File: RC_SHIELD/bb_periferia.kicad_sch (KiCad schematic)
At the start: 58 parts, among them J10 POWER_SUPPLY, J11 ALF_MOT_DRV, J11 GPIO1, J12 BET_MOT_DRV, J12 GPIO2, J13 SPI, J14 I2C_TEMP, J15 DOOR_SWITCH, J16 ESTOP, J17 FAN, J18 P5a, J9 P4a, Q1 BSS123, Q2 BSS123, U2 SN75LBC179AD, U3 ESP8266-01/ESP-01, U4 LCD-016N002L

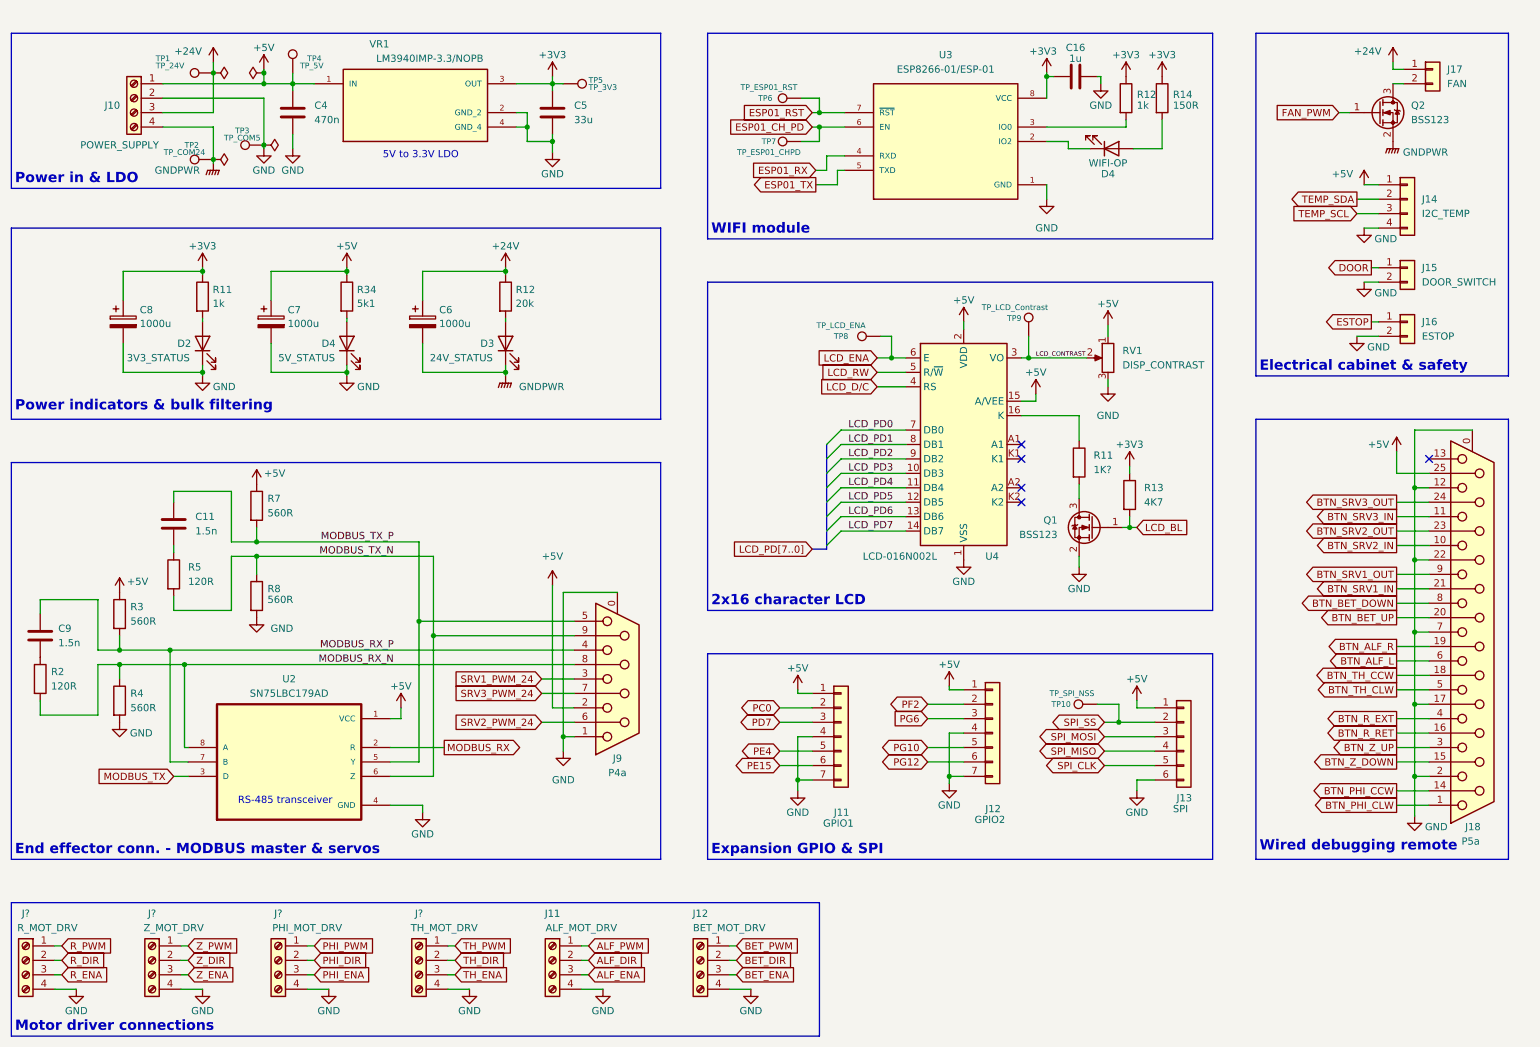
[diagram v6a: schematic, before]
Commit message: [SCH] updated power indicator LED resistor values and tidied up page 3
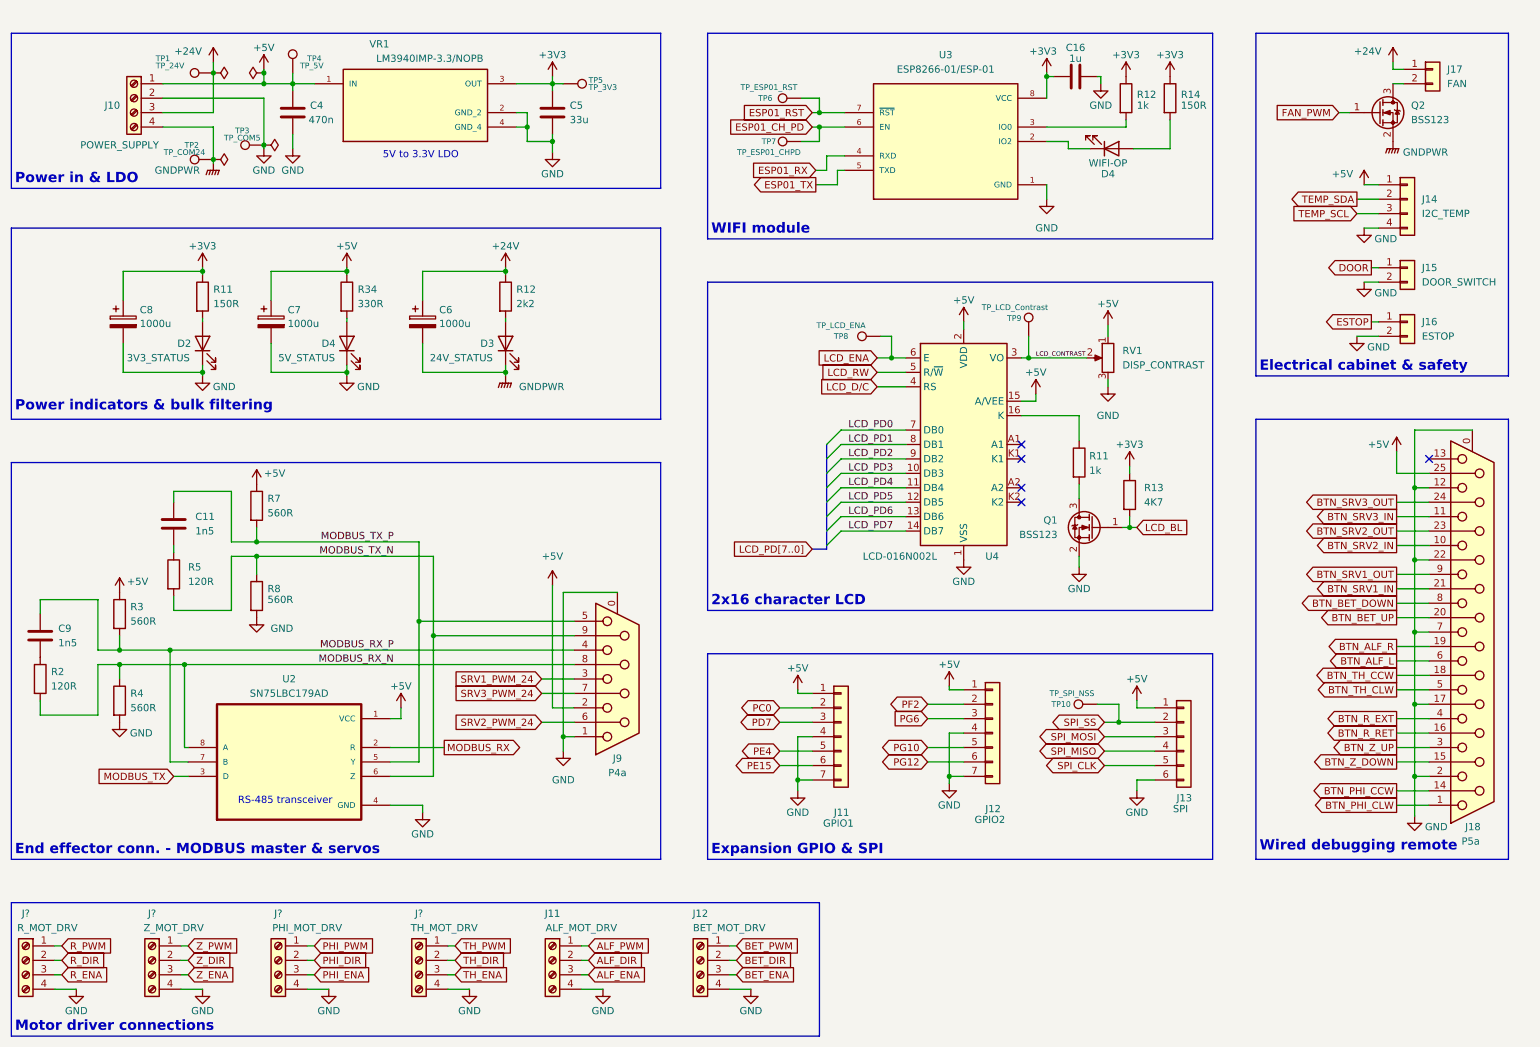
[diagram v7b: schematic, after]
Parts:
- C11, C9: value 1.5n -> 1n5
- D2, D3, D4: footprint Capacitor_SMD:C_0805_2012Metric_Pad1.18x1.45mm_HandSolder -> LED_SMD:LED_0805_2012Metric_Pad1.15x1.40mm_HandSolder
- R11: value 1K? -> 1k; now left out of the parts list
- R11: value 1k -> 150R
- R12: value 20k -> 2k2
- R34: value 5k1 -> 330R
- U3: symbol ESP8266-01_ESP-01:ESP8266-01/ESP-01 -> ESP8266-01_ESP-01:ESP8266-01/ESP-01
- VR1: symbol LM3940IMP-3.3_NOPB:LM3940IMP-3.3/NOPB -> LM3940IMP-3.3_NOPB:LM3940IMP-3.3/NOPB
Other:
- moved on the sheet: R14
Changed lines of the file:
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@@
     (stroke (width 0) (type default))
   )
-  (wire (pts (xy 219.075 31.75) (xy 219.075 36.83))
+  (wire (pts (xy 220.472 31.75) (xy 220.472 36.83))
     (stroke (width 0) (type default))
   )
@@
     (stroke (width 0) (type default))
   )
-  (wire (pts (xy 213.995 36.83) (xy 219.075 36.83))
+  (wire (pts (xy 213.995 36.83) (xy 220.472 36.83))
     (stroke (width 0) (type default))
   )
@@
       (effects (font (size 1.27 1.27)) (justify right))
     )
-    (property "Footprint" "Capacitor_SMD:C_0805_2012Metric_Pad1.18x1.45mm_HandSolder" (at 75.565 71.12 0)
+    (property "Footprint" "LED_SMD:LED_0805_2012Metric_Pad1.15x1.40mm_HandSolder" (at 75.565 71.12 0)
       (effects (font (size 1.27 1.27)) hide)
     )
@@
     )
   )
-  (symbol (lib_id "LM3940IMP-3.3_NOPB:LM3940IMP-3.3{slash}NOPB") (at 87.63 27.94 0) (unit 1)
+  (symbol (lib_id "LM3940IMP-3.3_NOPB:LM3940IMP-3.3/NOPB") (at 87.63 27.94 0) (unit 1)
     (in_bom yes) (on_board yes) (dnp no)
     (property "Reference" "VR1" (at 81.28 18.415 0)
@@
   (symbol (lib_id "Device:R") (at 75.565 62.865 0) (unit 1)
     (in_bom yes) (on_board yes) (dnp no) (fields_autoplaced)
-    (property "Reference" "R34" (at 77.343 61.6529 0)
+    (property "Reference" "R34" (at 77.47 61.595 0)
       (effects (font (size 1.27 1.27)) (justify left))
     )
-    (property "Value" "5k1" (at 77.343 64.0771 0)
+    (property "Value" "330R" (at 77.47 64.135 0)
       (effects (font (size 1.27 1.27)) (justify left))
     )
@@
     )
   )
-  (symbol (lib_id "Device:R") (at 219.075 27.94 0) (unit 1)
+  (symbol (lib_id "Device:R") (at 220.472 27.94 0) (unit 1)
     (in_bom yes) (on_board yes) (dnp no)
-    (property "Reference" "R14" (at 220.98 27.305 0)
+    (property "Reference" "R14" (at 222.377 27.305 0)
       (effects (font (size 1.27 1.27)) (justify left))
     )
-    (property "Value" "150R" (at 220.98 29.21 0)
+    (property "Value" "150R" (at 222.377 29.21 0)
       (effects (font (size 1.27 1.27)) (justify left))
     )
-    (property "Footprint" "Resistor_SMD:R_0805_2012Metric_Pad1.20x1.40mm_HandSolder" (at 217.297 27.94 90)
+    (property "Footprint" "Resistor_SMD:R_0805_2012Metric_Pad1.20x1.40mm_HandSolder" (at 218.694 27.94 90)
       (effects (font (size 1.27 1.27)) hide)
     )
-    (property "Datasheet" "~" (at 219.075 27.94 0)
+    (property "Datasheet" "~" (at 220.472 27.94 0)
       (effects (font (size 1.27 1.27)) hide)
     )
@@
   (symbol (lib_id "Device:R") (at 103.505 62.865 0) (unit 1)
     (in_bom yes) (on_board yes) (dnp no) (fields_autoplaced)
-    (property "Reference" "R12" (at 105.283 61.6529 0)
+    (property "Reference" "R12" (at 105.41 61.595 0)
       (effects (font (size 1.27 1.27)) (justify left))
     )
-    (property "Value" "20k" (at 105.283 64.0771 0)
+    (property "Value" "2k2" (at 105.41 64.135 0)
       (effects (font (size 1.27 1.27)) (justify left))
     )
@@
     )
   )
-  (symbol (lib_id "ESP8266-01_ESP-01:ESP8266-01{slash}ESP-01") (at 180.975 35.56 0) (unit 1)
+  (symbol (lib_id "ESP8266-01_ESP-01:ESP8266-01/ESP-01") (at 180.975 35.56 0) (unit 1)
     (in_bom yes) (on_board yes) (dnp no) (fields_autoplaced)
     (property "Reference" "U3" (at 180.975 20.32 0)
@@
       (effects (font (size 1.27 1.27)) (justify left))
     )
-    (property "Value" "1.5n" (at 24.765 123.825 0)
+    (property "Value" "1n5" (at 24.765 123.825 0)
       (effects (font (size 1.27 1.27)) (justify left))
     )
@@
     )
   )
-  (symbol (lib_id "power:+3V3") (at 219.075 24.13 0) (unit 1)
+  (symbol (lib_id "power:+3V3") (at 220.472 24.13 0) (unit 1)
     (in_bom yes) (on_board yes) (dnp no)
-    (property "Reference" "#PWR065" (at 219.075 27.94 0)
+    (property "Reference" "#PWR065" (at 220.472 27.94 0)
       (effects (font (size 1.27 1.27)) hide)
     )
-    (property "Value" "+3V3" (at 219.075 20.32 0)
+    (property "Value" "+3V3" (at 220.472 20.32 0)
       (effects (font (size 1.27 1.27)))
     )
-    (property "Footprint" "" (at 219.075 24.13 0)
+    (property "Footprint" "" (at 220.472 24.13 0)
       (effects (font (size 1.27 1.27)) hide)
     )
-    (property "Datasheet" "" (at 219.075 24.13 0)
+    (property "Datasheet" "" (at 220.472 24.13 0)
       (effects (font (size 1.27 1.27)) hide)
     )
@@
   )
   (symbol (lib_id "Device:C") (at 111.76 30.48 0) (unit 1)
-    (in_bom yes) (on_board yes) (dnp no) (fields_autoplaced)
-    (property "Reference" "C5" (at 115.57 29.21 0)
+    (in_bom yes) (on_board yes) (dnp no)
+    (property "Reference" "C5" (at 114.808 29.21 0)
       (effects (font (size 1.27 1.27)) (justify left))
     )
-    (property "Value" "33u" (at 115.57 31.75 0)
+    (property "Value" "33u" (at 114.808 31.75 0)
       (effects (font (size 1.27 1.27)) (justify left))
     )
@@
       (effects (font (size 1.27 1.27)))
     )
-    (property "Footprint" "Capacitor_SMD:C_0805_2012Metric_Pad1.18x1.45mm_HandSolder" (at 210.185 36.83 0)
+    (property "Footprint" "LED_SMD:LED_0805_2012Metric_Pad1.15x1.40mm_HandSolder" (at 210.185 36.83 0)
       (effects (font (size 1.27 1.27)) hide)
     )
@@
   )
   (symbol (lib_id "Device:R") (at 204.47 92.075 0) (unit 1)
-    (in_bom yes) (on_board yes) (dnp no) (fields_autoplaced)
-    (property "Reference" "R11" (at 207.01 90.805 0)
+    (in_bom no) (on_board yes) (dnp no)
+    (property "Reference" "R11" (at 206.248 90.932 0)
       (effects (font (size 1.27 1.27)) (justify left))
     )
-    (property "Value" "1K?" (at 207.01 93.345 0)
+    (property "Value" "1k" (at 206.248 93.472 0)
       (effects (font (size 1.27 1.27)) (justify left))
     )
@@
       (effects (font (size 1.27 1.27)) (justify right))
     )
-    (property "Footprint" "Capacitor_SMD:C_0805_2012Metric_Pad1.18x1.45mm_HandSolder" (at 50.165 71.12 0)
+    (property "Footprint" "LED_SMD:LED_0805_2012Metric_Pad1.15x1.40mm_HandSolder" (at 50.165 71.12 0)
       (effects (font (size 1.27 1.27)) hide)
     )
@@
   )
   (symbol (lib_id "Device:C") (at 66.04 30.48 0) (unit 1)
-    (in_bom yes) (on_board yes) (dnp no) (fields_autoplaced)
-    (property "Reference" "C4" (at 69.85 29.21 0)
+    (in_bom yes) (on_board yes) (dnp no)
+    (property "Reference" "C4" (at 69.088 29.21 0)
       (effects (font (size 1.27 1.27)) (justify left))
     )
-    (property "Value" "470n" (at 69.85 31.75 0)
+    (property "Value" "470n" (at 68.834 31.75 0)
       (effects (font (size 1.27 1.27)) (justify left))
     )
@@
   (symbol (lib_id "Device:R") (at 50.165 62.865 0) (unit 1)
     (in_bom yes) (on_board yes) (dnp no) (fields_autoplaced)
-    (property "Reference" "R11" (at 51.943 61.6529 0)
+    (property "Reference" "R11" (at 52.07 61.595 0)
       (effects (font (size 1.27 1.27)) (justify left))
     )
-    (property "Value" "1k" (at 51.943 64.0771 0)
+    (property "Value" "150R" (at 52.07 64.135 0)
       (effects (font (size 1.27 1.27)) (justify left))
     )
@@
       (effects (font (size 1.27 1.27)) (justify right))
     )
-    (property "Footprint" "Capacitor_SMD:C_0805_2012Metric_Pad1.18x1.45mm_HandSolder" (at 103.505 71.12 0)
+    (property "Footprint" "LED_SMD:LED_0805_2012Metric_Pad1.15x1.40mm_HandSolder" (at 103.505 71.12 0)
       (effects (font (size 1.27 1.27)) hide)
     )
@@
       (effects (font (size 1.27 1.27)) (justify left))
     )
-    (property "Value" "1.5n" (at 48.895 104.14 0)
+    (property "Value" "1n5" (at 48.895 104.14 0)
       (effects (font (size 1.27 1.27)) (justify left))
     )

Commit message: [SCH] added "exclude from BOM" signs
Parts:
- U3, U4: now left out of the parts list
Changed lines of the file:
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@@
   )
   (symbol (lib_id "ESP8266-01_ESP-01:ESP8266-01/ESP-01") (at 180.975 35.56 0) (unit 1)
-    (in_bom yes) (on_board yes) (dnp no) (fields_autoplaced)
+    (in_bom no) (on_board yes) (dnp no) (fields_autoplaced)
     (property "Reference" "U3" (at 180.975 20.32 0)
       (effects (font (size 1.27 1.27)))
@@
   )
   (symbol (lib_id "Display_Character:LCD-016N002L") (at 184.15 88.9 0) (unit 1)
-    (in_bom yes) (on_board yes) (dnp no)
+    (in_bom no) (on_board yes) (dnp no)
     (property "Reference" "U4" (at 187.96 108.585 0)
       (effects (font (size 1.27 1.27)) (justify left))
